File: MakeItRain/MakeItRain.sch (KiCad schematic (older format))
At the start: 19 parts, among them IC1 LM2597MX-5.0_NOPB, IC2 TL071CP, J10 Conn_01x15, J11 Conn_01x15, P1 Screw_Terminal_01x02, Q1 IRF9Z34NPBF, U1 178.6165.0001

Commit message: WIP to test some hardware designs.
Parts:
- removed IC2: TL071CP, SamacSys_Parts:DIP794W53P254L959H508Q8N, symbol SamacSys_Parts:TL071CP
- removed J10, J11: Conn_01x15, Connector_PinSocket_2.54mm:PinSocket_1x15_P2.54mm_Vertical, symbol Connector_Generic:Conn_01x15
- added IC2: OPA2340PA, DIP794W53P254L959H508Q8N, symbol SamacSys_Parts:OPA2340PA
- added J1, J2: Conn_01x19, Connector_PinSocket_2.54mm:PinSocket_1x19_P2.54mm_Vertical, symbol Connector_Generic:Conn_01x19
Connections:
- net labels added: +5V, 3.3V, 5V, CLK, P0, P15, P16, P17, P18, P19, P2, P21, P22, P23, P4, P5, RX, SD1, SD2, SD3, SDD, SVN, SVP, TX
- net labels removed: 3v3, D15, D18, D19, D2, D21, D22, D23, D4, D5, RX0, RX2, TX0, TX2, VN, VP, Vin
- wire segments 61 -> 122
- no-connect marks 2 -> 17
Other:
- moved on the sheet: IC1, R26, R27, R28

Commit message: wip for layout
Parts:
- removed J1: Conn_01x19, Connector_PinSocket_2.54mm:PinSocket_1x19_P2.54mm_Vertical, symbol Connector_Generic:Conn_01x19
- removed Z1, Z2, Z3, Z4, Z5, Z6, Z7, Z8: Screw_Terminal_01x02, TerminalBlock_Phoenix:TerminalBlock_Phoenix_MKDS-1,5-2-5.08_1x02_P5.08mm_Horizontal, symbol Connector:Screw_Terminal_01x02
- added C1, C2: 0.1uF, Capacitor_THT:C_Disc_D4.7mm_W2.5mm_P5.00mm, symbol Device:C
- added C3, C4: CP1, Capacitor_THT:CP_Radial_D8.0mm_P3.50mm, symbol Device:CP1
- added D1: 1N5817, Diode_THT:D_DO-41_SOD81_P10.16mm_Horizontal, symbol Diode:1N5817
- added J1: Conn_02x16_Odd_Even, Connector_PinHeader_2.54mm:PinHeader_2x16_P2.54mm_Vertical, symbol Connector_Generic:Conn_02x16_Odd_Even
- added J2: Conn_02x19_Odd_Even, Connector_PinSocket_2.54mm:PinSocket_2x19_P2.54mm_Vertical, symbol Connector_Generic:Conn_02x19_Odd_Even
- added L1: 150uH, Inductor_THT:L_Axial_L6.6mm_D2.7mm_P10.16mm_Horizontal_Vishay_IM-2, symbol Device:L
- added R2: 22k, Resistor_THT:R_Axial_DIN0207_L6.3mm_D2.5mm_P5.08mm_Vertical, symbol Device:R
- added R6: 10k, Resistor_THT:R_Axial_DIN0207_L6.3mm_D2.5mm_P5.08mm_Vertical, symbol Device:R
- added Z1, Z2, Z3, Z4: Screw_Terminal_01x03, TerminalBlock_Phoenix:TerminalBlock_Phoenix_MKDS-1,5-3-5.08_1x03_P5.08mm_Horizontal, symbol Connector:Screw_Terminal_01x03
- IC1: renamed from IC2; footprint DIP794W53P254L959H508Q8N -> SamacSys_Parts:DIP794W53P254L959H508Q8N
- R3: renamed from R26; value R -> 120k
- R4: renamed from R27; value R -> 22k
- R5: renamed from R28; value R -> 47k
- renumbered IC1 to IC2, J2 to J3
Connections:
- net +3V3: now also J1.2 (Pin_2), J1.4 (Pin_4), J1.6 (Pin_6), J2.1 (Pin_1), J2.2 (Pin_2)
- net +5V: now also IC2.3 (BIAS_SUPPLY), IC2.4 (FEEDBACK), C4.1, J2.37 (Pin_37), J2.38 (Pin_38), L1.2
- net +VDC: now also IC2.7 (+VIN), C3.1, J1.1 (Pin_1), J1.11 (Pin_11), J1.13 (Pin_13), J1.15 (Pin_15), J1.3 (Pin_3), J1.5 (Pin_5), J1.7 (Pin_7), J1.9 (Pin_9), R6.1
- net D12: now also J2.25 (Pin_25), J2.26 (Pin_26)
- net D13: now also J2.29 (Pin_29), J2.30 (Pin_30)
- net D14: now also J2.23 (Pin_23), J2.24 (Pin_24)
- net D25: now also J1.16 (Pin_16), J2.17 (Pin_17), J2.18 (Pin_18)
- net D26: now also J1.20 (Pin_20), J2.19 (Pin_19), J2.20 (Pin_20)
- net D27: now also J2.21 (Pin_21), J2.22 (Pin_22)
- net D32: now also J1.8 (Pin_8), J2.13 (Pin_13), J2.14 (Pin_14)
- net D33: now also J1.12 (Pin_12), J2.15 (Pin_15), J2.16 (Pin_16)
- net D34: now also J2.10 (Pin_10), J2.9 (Pin_9)
- net D35: now also J2.11 (Pin_11), J2.12 (Pin_12)
- net EN: now also J2.3 (Pin_3), J2.4 (Pin_4)
- net GND: now also IC2.6 (GROUND), C1.2, C2.2, C3.2, C4.2, D1.2 (A), J1.17 (Pin_17), J1.19 (Pin_19), J1.21 (Pin_21), J1.23 (Pin_23), J1.25 (Pin_25), J1.27 (Pin_27), J1.29 (Pin_29), J1.31 (Pin_31), J2.27 (Pin_27), J2.28 (Pin_28), J2.35 (Pin_35), J2.36 (Pin_36), R2.2, Z1.3 (Pin_3), Z2.3 (Pin_3), Z3.3 (Pin_3), Z4.3 (Pin_3)
- net P0: now also J1.30 (Pin_30)
- net P16: now also J1.28 (Pin_28)
- net P17: now also J1.26 (Pin_26)
- net P18: now also J1.22 (Pin_22)
- net P19: now also J1.18 (Pin_18)
- net P2: now also J1.32 (Pin_32), R2.1
- net P21: now also J1.14 (Pin_14)
- net P22: now also J1.10 (Pin_10)
- net P5: now also J1.24 (Pin_24)
- net SD2: now also J2.31 (Pin_31), J2.32 (Pin_32)
- net SD3: now also J2.33 (Pin_33), J2.34 (Pin_34)
- net SVN: now also J2.7 (Pin_7), J2.8 (Pin_8)
- net SVP: now also J2.5 (Pin_5), J2.6 (Pin_6)
- net Zone1IO/ZoneInput: now also Z1.1 (Pin_1)
- net Zone2IO/ZoneInput: now also Z2.1 (Pin_1)
- net Zone3IO/ZoneInput: now also Z3.1 (Pin_1)
- net Zone4IO/ZoneInput: now also Z4.1 (Pin_1)
- net at IC2.1 (ERROR_FLAG): now also R6.2
- net at IC2.2 (DELAY): now also C1.1
- net at IC2.5 (~SHUTDOWN~/SOFT-START): now also C2.1
- net at IC2.8 (OUTPUT): now also D1.1 (K), L1.1
- new net Zone1IO/ZoneOutput: Z1.2 (Pin_2)
- new net Zone2IO/ZoneOutput: Z2.2 (Pin_2)
- new net Zone3IO/ZoneOutput: Z3.2 (Pin_2)
- new net Zone4IO/ZoneOutput: Z4.2 (Pin_2)
- no-connect marks 17 -> 14
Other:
- moved on the sheet: IC1, IC2, J3, P1, Q1, R1, R3, R4, R5, U1

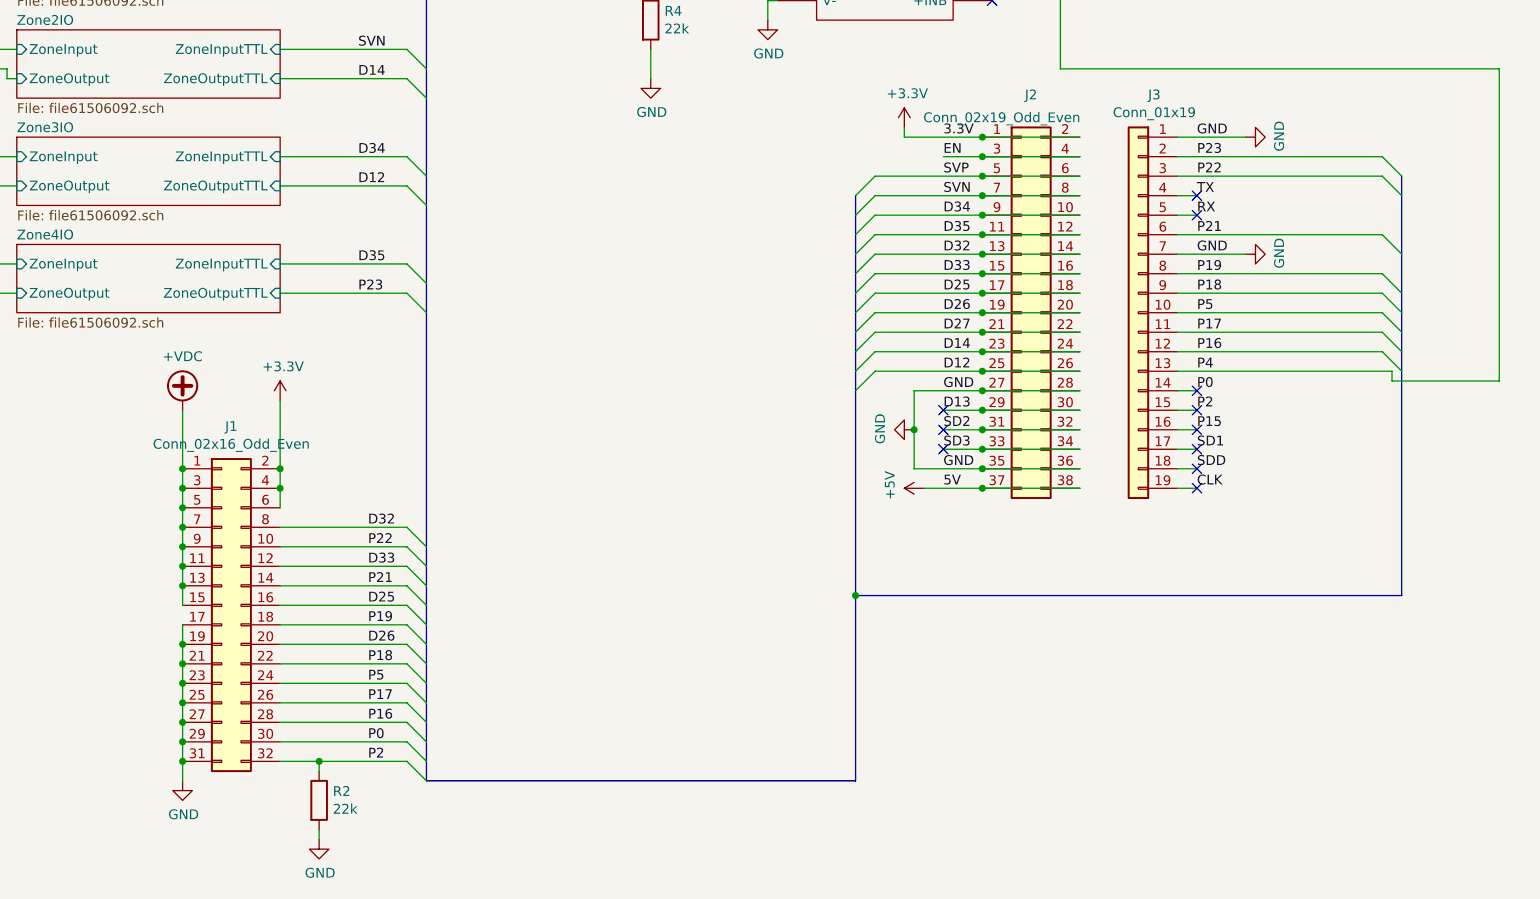
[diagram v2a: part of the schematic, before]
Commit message: updated to have only up to 4 additional zones with a separate board.
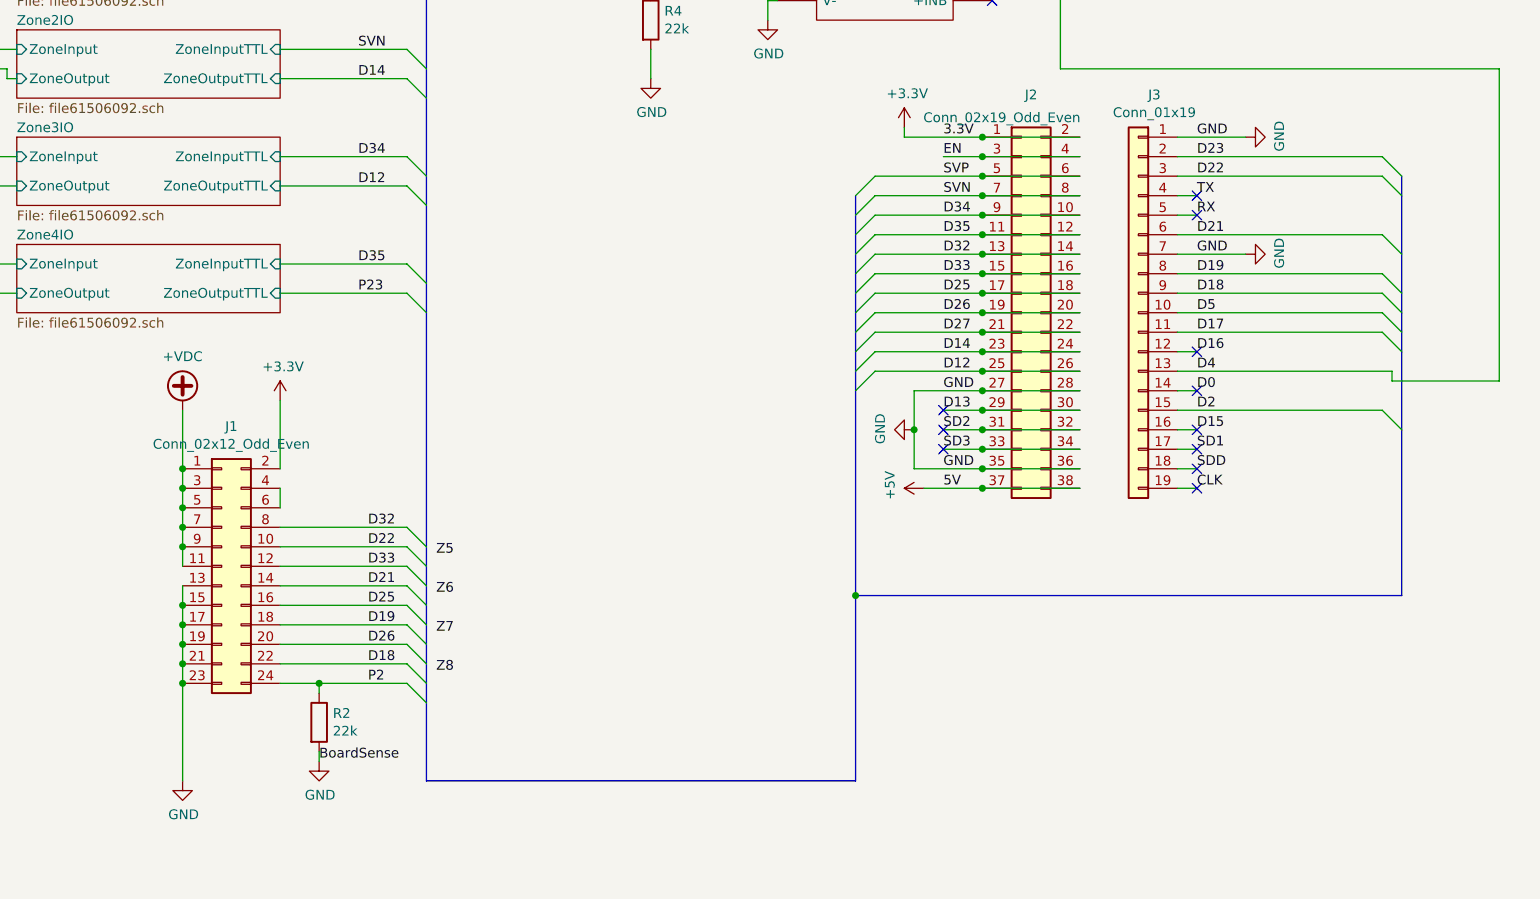
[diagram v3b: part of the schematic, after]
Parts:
- removed J1: Conn_02x16_Odd_Even, Connector_PinHeader_2.54mm:PinHeader_2x16_P2.54mm_Vertical, symbol Connector_Generic:Conn_02x16_Odd_Even
- added J1: Conn_02x12_Odd_Even, Connector_PinHeader_2.54mm:PinHeader_2x12_P2.54mm_Vertical, symbol Connector_Generic:Conn_02x12_Odd_Even
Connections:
- net +3V3: now also J1.2 (Pin_2)
- net +VDC: now also J1.1 (Pin_1), J1.11 (Pin_11), J1.3 (Pin_3), J1.5 (Pin_5), J1.7 (Pin_7), J1.9 (Pin_9)
- net D25: now also J1.16 (Pin_16)
- net D26: now also J1.20 (Pin_20)
- net D32: now also J1.8 (Pin_8)
- net D33: now also J1.12 (Pin_12)
- net GND: now also J1.13 (Pin_13), J1.15 (Pin_15), J1.17 (Pin_17), J1.19 (Pin_19), J1.21 (Pin_21), J1.23 (Pin_23)
- net P2: now also J1.24 (Pin_24); no longer J3.15 (Pin_15)
- net P23: no longer J3.2 (Pin_2)
- net P0 renamed D0
- net P15 renamed D15
- net P16 renamed D16
- net P17 renamed D17
- net P18 renamed D18
- net D18: now also J1.22 (Pin_22)
- net P19 renamed D19
- net D19: now also J1.18 (Pin_18)
- net P21 renamed D21
- net D21: now also J1.14 (Pin_14)
- net P22 renamed D22
- net D22: now also J1.10 (Pin_10)
- net P4 renamed D4
- net P5 renamed D5
- new net: J1.4 (Pin_4), J1.6 (Pin_6)
- new net D2: J3.15 (Pin_15)
- new net D23: J3.2 (Pin_2)
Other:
- moved on the sheet: R2
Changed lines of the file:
@@
 GND
 Text Label 8600 4200 0    50   ~ 0
-P23
+D23
 Text Label 8600 4300 0    50   ~ 0
-P22
+D22
 Text Label 8600 5900 0    50   ~ 0
 CLK
@@
 SD1
 Text Label 8600 5600 0    50   ~ 0
-P15
+D15
 Text Label 8600 5500 0    50   ~ 0
-P2
+D2
 Text Label 8600 5400 0    50   ~ 0
-P0
-Text Label 8600 5300 0    50   ~ 0
-P4
-Text Label 8600 5200 0    50   ~ 0
-P16
+D0
 Text Label 8600 5100 0    50   ~ 0
-P17
+D17
 Text Label 8600 5000 0    50   ~ 0
-P5
+D5
 Text Label 8600 4900 0    50   ~ 0
-P18
+D18
 Text Label 8600 4800 0    50   ~ 0
-P19
+D19
 Text Label 8600 4700 0    50   ~ 0
 GND
 Text Label 8600 4600 0    50   ~ 0
-P21
+D21
 Text Label 8600 4500 0    50   ~ 0
 RX
@@
 	8500 5600 8600 5600
 Wire Wire Line
-	8600 5500 8500 5500
-Wire Wire Line
 	8500 5400 8600 5400
 Wire Wire Line
@@
 Wire Wire Line
 	8500 5000 9550 5000
-Entry Wire Line
-	9550 5200 9650 5300
-Wire Wire Line
-	8500 5200 9550 5200
-Wire Wire Line
-	8500 5300 9600 5300
-Wire Wire Line
-	9600 5300 9600 5350
 Wire Wire Line
 	9600 5350 10150 5350
@@
 	4650 7400 6850 7400
 Entry Wire Line
-	4550 7200 4650 7300
-Entry Wire Line
-	4550 7300 4650 7400
-Text Label 4350 7200 0    50   ~ 0
-P0
-Text Label 4350 7300 0    50   ~ 0
+	4550 6900 4650 7000
+Text Label 4350 6900 0    50   ~ 0
 P2
-Entry Wire Line
-	4550 6900 4650 7000
-Entry Wire Line
-	4550 7100 4650 7200
-Entry Wire Line
-	4550 7000 4650 7100
-Text Label 4350 6900 0    50   ~ 0
-P5
-Text Label 4350 7000 0    50   ~ 0
-P17
-Text Label 4350 7100 0    50   ~ 0
-P16
 Text Label 4350 6400 0    50   ~ 0
-P21
+D21
 Text Label 4350 6600 0    50   ~ 0
-P19
+D19
 Text Label 4350 6800 0    50   ~ 0
-P18
+D18
 Text Label 4350 6200 0    50   ~ 0
-P22
+D22
 Text Label 4350 6100 0    50   ~ 0
 D32
@@
 D26
 Entry Wire Line
-	4550 6800 4650 6900
-Entry Wire Line
 	4550 6700 4650 6800
 Entry Wire Line
@@
 Wire Wire Line
 	3900 6100 4550 6100
-$Comp
-L Connector_Generic:Conn_02x16_Odd_Even J1
-U 1 1 615C7BFA
-P 3600 6500
-F 0 "J1" H 3650 7417 50  0000 C CNN
-F 1 "Conn_02x16_Odd_Even" H 3650 7326 50  0000 C CNN
-F 2 "Connector_PinHeader_2.54mm:PinHeader_2x16_P2.54mm_Vertical" H 3600 6500 50  0001 C CNN
-F 3 "~" H 3600 6500 50  0001 C CNN
-	1    3600 6500
-	1    0    0    -1
-$EndComp
 $Comp
 L power:GND #PWR?
@@
 	1    0    0    -1
 $EndComp
-Wire Wire Line
-	3400 7400 3400 7300
 $Comp
 L power:GND #PWR?
@@
 $EndComp
 Wire Wire Line
-	4550 7300 4100 7300
-Wire Wire Line
-	3900 7200 4550 7200
-Wire Wire Line
-	4550 7100 3900 7100
-Wire Wire Line
-	3900 7000 4550 7000
-Wire Wire Line
-	4550 6900 3900 6900
+	4550 6900 4100 6900
 $Comp
 L power:+3.3V #PWR010
@@
 	1    0    0    -1
 $EndComp
+$Comp
+L Device:R R?
+U 1 1 619FD932
+P 4100 7100
+AR Path="/6158F2C4/619FD932" Ref="R?"  Part="1"
+AR Path="/619FD932" Ref="R2"  Part="1"
+F 0 "R2" H 4170 7146 50  0000 L CNN
+F 1 "22k" H 4170 7055 50  0000 L CNN
+F 2 "Resistor_THT:R_Axial_DIN0207_L6.3mm_D2.5mm_P5.08mm_Vertical" V 4030 7100 50  0001 C CNN
+F 3 "~" H 4100 7100 50  0001 C CNN
+	1    4100 7100
+	1    0    0    -1
+$EndComp
+$Comp
+L power:GND #PWR?
+U 1 1 619FD938
+P 4100 7300
+AR Path="/6158F2C4/619FD938" Ref="#PWR?"  Part="1"
+AR Path="/619FD938" Ref="#PWR011"  Part="1"
+F 0 "#PWR011" H 4100 7050 50  0001 C CNN
+F 1 "GND" H 4105 7127 50  0000 C CNN
+F 2 "" H 4100 7300 50  0001 C CNN
+F 3 "" H 4100 7300 50  0001 C CNN
+	1    4100 7300
+	1    0    0    -1
+$EndComp
+Wire Wire Line
+	4100 7250 4100 7300
+Wire Wire Line
+	4100 6950 4100 6900
+Connection ~ 4100 6900
+Wire Wire Line
+	4100 6900 3900 6900
+NoConn ~ 8600 5400
+Text Label 4700 6250 0    50   ~ 0
+Z5
+Text Label 4700 6450 0    50   ~ 0
+Z6
+Text Label 4700 6650 0    50   ~ 0
+Z7
+Text Label 4700 6850 0    50   ~ 0
+Z8
+Text Label 4100 7300 0    50   ~ 0
+BoardSense
+Text Label 8600 5200 0    50   ~ 0
+D16
+Text Label 8600 5300 0    50   ~ 0
+D4
+Wire Wire Line
+	8500 5300 9600 5300
+Wire Wire Line
+	9600 5300 9600 5350
+Wire Wire Line
+	8500 5200 8600 5200
+Entry Wire Line
+	9550 5500 9650 5600
+Wire Wire Line
+	8500 5500 9550 5500
+NoConn ~ 8600 5200
+Entry Wire Line
+	4550 6800 4650 6900
+$Comp
+L Connector_Generic:Conn_02x12_Odd_Even J1
+U 1 1 6164B72D
+P 3600 6300
+F 0 "J1" H 3650 7017 50  0000 C CNN
+F 1 "Conn_02x12_Odd_Even" H 3650 6926 50  0000 C CNN
+F 2 "Connector_PinHeader_2.54mm:PinHeader_2x12_P2.54mm_Vertical" H 3600 6300 50  0001 C CNN
+F 3 "~" H 3600 6300 50  0001 C CNN
+	1    3600 6300
+	1    0    0    -1
+$EndComp
 Wire Wire Line
 	3900 5450 3900 5800
 Wire Wire Line
-	3900 5900 3900 5800
-Connection ~ 3900 5800
-Wire Wire Line
-	3900 6000 3900 5900
-Connection ~ 3900 5900
-Wire Wire Line
-	3400 7300 3400 7200
-Connection ~ 3400 7300
-Wire Wire Line
-	3400 7200 3400 7100
-Connection ~ 3400 7200
-Wire Wire Line
-	3400 7100 3400 7000
-Connection ~ 3400 7100
-Wire Wire Line
-	3400 7000 3400 6900
-Connection ~ 3400 7000
+	3400 5500 3400 5800
+Wire Wire Line
+	3900 5900 3900 6000
+Wire Wire Line
+	3400 6900 3400 7400
+Wire Wire Line
+	3400 5800 3400 5900
+Connection ~ 3400 5800
+Wire Wire Line
+	3400 5900 3400 6000
+Connection ~ 3400 5900
+Wire Wire Line
+	3400 6000 3400 6100
+Connection ~ 3400 6000
+Wire Wire Line
+	3400 6100 3400 6200
+Connection ~ 3400 6100
 Wire Wire Line
 	3400 6900 3400 6800
@@
 Connection ~ 3400 6700
 Wire Wire Line
-	3400 5500 3400 5800
-Wire Wire Line
-	3400 5800 3400 5900
-Connection ~ 3400 5800
-Wire Wire Line
-	3400 5900 3400 6000
-Connection ~ 3400 5900
-Wire Wire Line
-	3400 6100 3400 6000
-Connection ~ 3400 6000
-Wire Wire Line
-	3400 6200 3400 6100
-Connection ~ 3400 6100
+	3400 6600 3400 6500
+Connection ~ 3400 6600
+Wire Wire Line
+	3400 6500 3400 6400
+Connection ~ 3400 6500
 Wire Wire Line
 	3400 6300 3400 6200
 Connection ~ 3400 6200
-Wire Wire Line
-	3400 6400 3400 6300
-Connection ~ 3400 6300
-Wire Wire Line
-	3400 6500 3400 6400
-Connection ~ 3400 6400
-$Comp
-L Device:R R?
-U 1 1 619FD932
-P 4100 7500
-AR Path="/6158F2C4/619FD932" Ref="R?"  Part="1"
-AR Path="/619FD932" Ref="R2"  Part="1"
-F 0 "R2" H 4170 7546 50  0000 L CNN
-F 1 "22k" H 4170 7455 50  0000 L CNN
-F 2 "Resistor_THT:R_Axial_DIN0207_L6.3mm_D2.5mm_P5.08mm_Vertical" V 4030 7500 50  0001 C CNN
-F 3 "~" H 4100 7500 50  0001 C CNN
-	1    4100 7500
-	1    0    0    -1
-$EndComp
-$Comp
-L power:GND #PWR?
-U 1 1 619FD938
-P 4100 7700
-AR Path="/6158F2C4/619FD938" Ref="#PWR?"  Part="1"
-AR Path="/619FD938" Ref="#PWR011"  Part="1"
-F 0 "#PWR011" H 4100 7450 50  0001 C CNN
-F 1 "GND" H 4105 7527 50  0000 C CNN
-F 2 "" H 4100 7700 50  0001 C CNN
-F 3 "" H 4100 7700 50  0001 C CNN
-	1    4100 7700
-	1    0    0    -1
-$EndComp
-Wire Wire Line
-	4100 7650 4100 7700
-Wire Wire Line
-	4100 7350 4100 7300
-Connection ~ 4100 7300
-Wire Wire Line
-	4100 7300 3900 7300
-NoConn ~ 8600 5400
-NoConn ~ 8600 5500
 Wire Bus Line
 	9650 4300 9650 6450
